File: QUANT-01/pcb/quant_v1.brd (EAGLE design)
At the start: 127 x 81.3 mm, 59 parts, among them SW1 SUBMINI_SPDT, SW2 SUBMINI_SPDT, SW3 SUBMINI_SPDT, SW4 SUBMINI_SPDT, SW5_MODE SUBMINI_SPDT, U3 MCP6002, U4 TL074_

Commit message: started wiring.
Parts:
- added J3, J4, J5, J6: (no value), SparkFun-Connectors:1X09
- added R15, R16, R22, R23: 10k, SparkFun-Resistors:AXIAL-0.3
- CV_OUT: value THONKICONNNEW -> CV_OUT
- moved GATE_OUT 183.2 mm to (116.8, 61.0), turned to 90 degrees
- moved VR1 177.6 mm to (96.5, 71.1), turned to 270 degrees
- moved CV_OUT 170.7 mm to (116.8, 50.8), turned to 90 degrees
- moved CV_INPUT 167.4 mm to (116.8, 71.1), turned to 90 degrees
- moved D11 147.5 mm to (106.7, 61.0)
- moved SW4 142.5 mm to (71.1, 61.0)
- moved R8 134.6 mm to (76.2, 71.1), turned to 270 degrees
- moved SW5_MODE 134.6 mm to (99.1, 50.8)
- moved SW3 123.5 mm to (61.0, 61.0)
- moved D10 116.9 mm to (81.3, 71.1)
- moved R7 114.3 mm to (66.0, 71.1), turned to 270 degrees
- moved D5 107.2 mm to (30.5, 71.1)
- moved SW2 104.5 mm to (50.8, 61.0)
- moved D9 101.6 mm to (71.1, 71.1)
- moved R6 94.0 mm to (55.9, 71.1), turned to 270 degrees
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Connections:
- net N$21 renamed GLIDE_WIPER
- net N$23 renamed GLIDE_1
- removed net N$26: B1.18, R13.P$2
- removed net N$33: D11.A, R14.P$1, U4.14
- removed net VEE: B1.17, R12.P$1, U3.1
- new net -12V: U4.11
- new net CV_IN: B1.18, J5.4, R12.P$1, U3.1
- new net CV_INPUT: R9.P$1
- new net CV_OUT: J5.2, U4.8, U4.9
- new net GATE_LED: J5.1, R14.P$1, U4.14
- new net GATE_OUT: J5.3, R21.P$1
- new net LED_I: B1.12, J3.1, J4.1, R1.P$2
- new net LED_II: B1.11, J3.2, J4.2, R2.P$2
- new net LED_III: B1.10, J3.3, J4.3, R3.P$2
- new net LED_IV: B1.9, J3.4, J4.4, R4.P$2
- new net LED_V: B1.8, J3.5, J4.5, R5.P$2
- new net LED_VI: B1.7, J3.6, J4.6, R6.P$2
- new net LED_VII: B1.6, J3.7, J4.7, R7.P$2
- new net LED_VIII: B1.5, J3.8, J4.8, R8.P$2
- new net N$21: GATE_OUT.P$1_TIP, J6.3
- new net N$23: D11.A, J6.1
- new net SW_MODE: B1.17, J5.5
- net +12V: now also B1.24, C6.1, C9.1, D1.C, U4.4
- net 5V: now also J1.1, J2.1; no longer B1.24, C6.1, C9.1, D1.C, U4.11, U4.4
- net GND: now also J3.9, J4.9; no longer MPR121_TOUCH_PINS.1
- net N$10: now also CV_INPUT.P$1_TIP, J6.4; no longer B1.10, R6.P$2
- net N$11: now also J6.7, R16.P$2; no longer B1.11, R7.P$2
- net N$12: now also J6.6, R15.P$2; no longer B1.12, R8.P$2
- net N$22: now also CV_OUT.P$1_TIP, J6.2; no longer CV_INPUT.P$1_TIP, R9.P$1
- net N$25: now also J6.8, R22.P$2; no longer CV_OUT.P$1_TIP, U4.8, U4.9
- net N$31: now also J6.5, R13.P$2; no longer GATE_OUT.P$1_TIP, R21.P$1
- net N$4: now also R23.P$1, SW1.COM; no longer B1.5, R1.P$2
- net N$6: now also R22.P$1, SW2.COM; no longer B1.6, R2.P$2
- net N$7: now also R16.P$1, SW3.COM; no longer B1.7, R3.P$2
- net N$8: now also R15.P$1, SW4.COM; no longer B1.8, R4.P$2
- net N$9: now also J6.9, R23.P$2; no longer B1.9, R5.P$2
- net SW1: now also J5.9; no longer SW4.COM
- net SW2: now also J5.8; no longer SW3.COM
- net SW3: now also J5.7; no longer SW2.COM
- net SW4: now also J5.6; no longer SW1.COM
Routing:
- net +12V: track 0.00 -> 81.5 mm
- net LED_VIII: track 0.00 -> 5.08 mm
- net LED_VII: track 0.00 -> 5.08 mm
- net LED_VI: track 0.00 -> 5.08 mm
- net LED_V: track 0.00 -> 5.08 mm
- net LED_IV: track 0.00 -> 5.08 mm
- net LED_III: track 0.00 -> 5.08 mm
- net LED_II: track 0.00 -> 5.08 mm
- net LED_I: track 0.00 -> 5.08 mm
- net GND: track 0.00 -> 5.08 mm

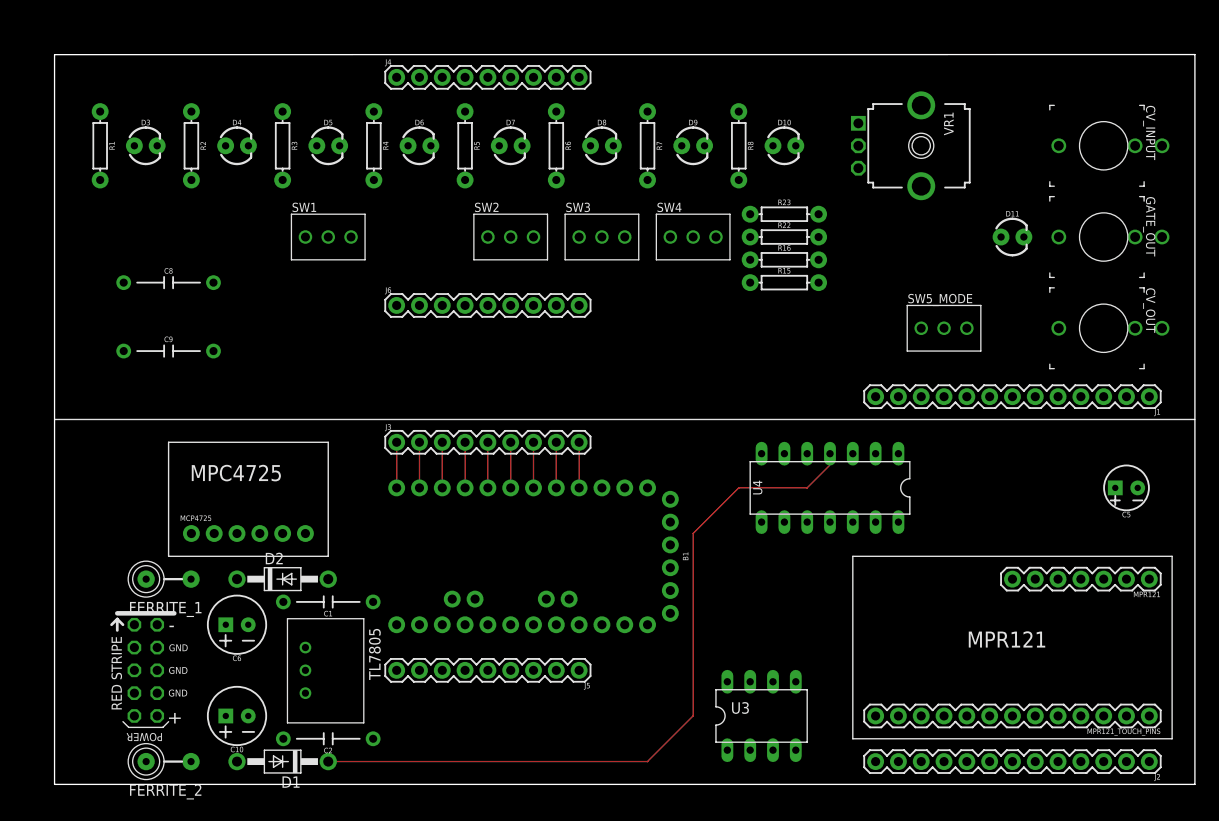
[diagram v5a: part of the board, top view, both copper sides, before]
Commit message: starting wiring. completed layout of components.
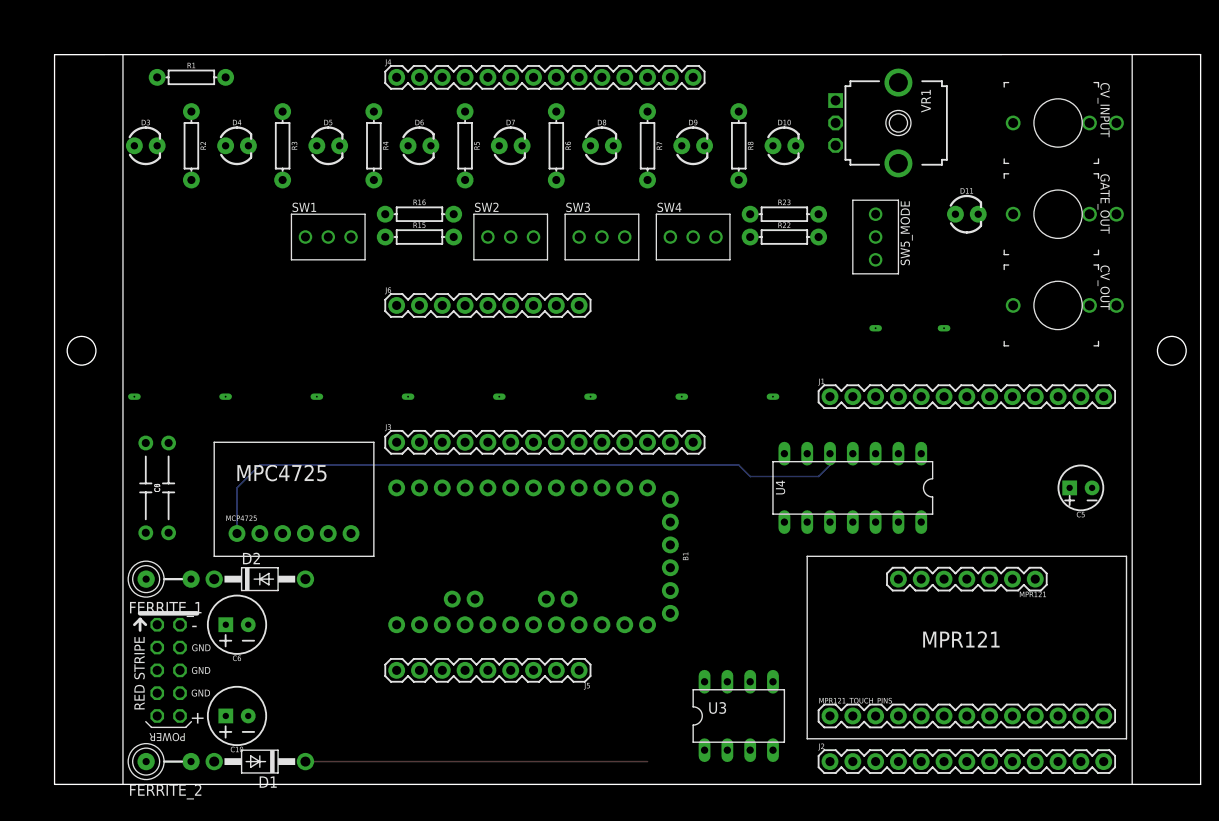
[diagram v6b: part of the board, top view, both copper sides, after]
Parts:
- removed C1: 0.33uF, SparkFun-Capacitors:CAP-PTH-10MM
- removed C2: 0.1uF, SparkFun-Capacitors:CAP-PTH-10MM
- removed TL7805: (no value), SparkFun-IC-Power:DC-DC_CONVERTER_78XX
- added TOUCH_I, TOUCH_II, TOUCH_III, TOUCH_IV, TOUCH_V, TOUCH_VI, TOUCH_VII: (no value), ESSY:TOUCH_PAD_ESSY
- added TOUCH_VIII: touch_8, ESSY:TOUCH_PAD_ESSY
- added U$1, U$2: (no value), ESSY:TOUCH_PAD_INCREMENT
- added U$3, U$4: (no value), ESSY:EURO_PANEL_SCREW_HOLE
- J3, J4: device SparkFun-Connectors:1X09 -> SparkFun-Connectors:1X14
- moved R15 41.0 mm to (40.6, 61.0)
- moved R16 41.0 mm to (40.6, 63.5)
- moved J1 35.6 mm to (86.4, 43.2), turned to 0 degrees
- moved J2 35.6 mm to (86.4, 2.54), turned to 0 degrees
- moved MPR121_TOUCH_PINS 35.6 mm to (86.4, 7.62), turned to 0 degrees
- moved C8 22.9 mm to (12.7, 33.0), turned to 90 degrees
- moved C9 15.5 mm to (10.2, 33.0), turned to 270 degrees
- moved SW5_MODE 12.7 mm to (91.4, 61.0), turned to 270 degrees
- moved MPR121 12.7 mm to (109.2, 22.9)
- moved R1 12.7 mm to (15.2, 78.7), turned to 0 degrees
- moved D11 5.68 mm to (101.6, 63.5)
- moved CV_OUT 5.68 mm to (111.8, 53.3)
- moved GATE_OUT 5.68 mm to (111.8, 63.5)
- moved CV_INPUT 5.68 mm to (111.8, 73.7)
- moved MCP4725 5.08 mm to (20.3, 27.9)
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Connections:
- removed net GLIDE_WIPER: U4.6, U4.7, VR1.2, VR1.3
- new net GLIDE_3: J3.11, U4.6, U4.7
- new net N$26: J4.8, R8.P$2
- new net N$33: J4.7, R7.P$2
- new net N$35: J4.6, R6.P$2
- new net N$36: J4.5, R5.P$2
- new net N$40: J4.4, R4.P$2
- new net N$41: J4.3, R3.P$2
- new net N$42: J4.2, R2.P$2
- new net N$43: J4.1, R1.P$2
- new net N$44: J1.2, TOUCH_I.P$1
- new net N$45: J1.3, TOUCH_II.P$1
- new net N$46: J1.4, TOUCH_III.P$1
- new net N$47: J1.5, TOUCH_IV.P$1
- new net N$48: J1.6, TOUCH_V.P$1
- new net N$49: J1.7, TOUCH_VI.P$1
- new net N$50: J1.8, TOUCH_VII.P$1
- new net N$51: J1.9, TOUCH_VIII.P$1
- new net N$52: J1.10, U$2.P$1
- new net N$53: J1.11, U$1.P$1
- new net TO_GLIDE_1: J4.10, VR1.1
- new net TO_GLIDE_3: J4.11, VR1.2, VR1.3
- net +12V: no longer C1.1, TL7805.VIN
- net 5V: no longer C2.1, TL7805.VOUT
- net GLIDE_1: now also J3.10; no longer VR1.1
- net GND: no longer C1.2, C2.2, TL7805.GND
- net LED_I: no longer J4.1, R1.P$2
- net LED_II: no longer J4.2, R2.P$2
- net LED_III: no longer J4.3, R3.P$2
- net LED_IV: no longer J4.4, R4.P$2
- net LED_V: no longer J4.5, R5.P$2
- net LED_VI: no longer J4.6, R6.P$2
- net LED_VII: no longer J4.7, R7.P$2
- net LED_VIII: no longer J4.8, R8.P$2
- net TOUCH0: no longer J1.2
- net TOUCH1: no longer J1.3
- net TOUCH10: no longer J1.12
- net TOUCH11: no longer J1.13
- net TOUCH2: no longer J1.4
- net TOUCH3: no longer J1.5
- net TOUCH4: no longer J1.6
- net TOUCH5: no longer J1.7
- net TOUCH6: no longer J1.8
- net TOUCH7: no longer J1.9
- net TOUCH8: no longer J1.10
- net TOUCH9: no longer J1.11
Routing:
- net N$20: track 0.00 -> 74.5 mm
- net +12V: track 81.5 -> 38.1 mm
- net LED_VIII: track 5.08 -> 0.00 mm
- net LED_VII: track 5.08 -> 0.00 mm
- net LED_VI: track 5.08 -> 0.00 mm
- net LED_V: track 5.08 -> 0.00 mm
- net LED_IV: track 5.08 -> 0.00 mm
- net LED_III: track 5.08 -> 0.00 mm
- net LED_II: track 5.08 -> 0.00 mm
- net LED_I: track 5.08 -> 0.00 mm
- net GND: track 5.08 -> 0.00 mm
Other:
- board size 127 x 81.3 mm -> 127.6 x 81.3 mm
